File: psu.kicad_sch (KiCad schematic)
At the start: 8 parts, among them J2 USB_C_Receptacle_PowerOnly_6P, Q3 TIP125, Q4 TIP122

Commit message: Progress.
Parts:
- removed C7: 100n, Capacitor_SMD:C_0603_1608Metric_Pad1.08x0.95mm_HandSolder, symbol Device:C
- removed Q3: TIP125, Package_TO_SOT_THT:TO-220-3_Vertical, symbol Transistor_BJT:TIP125
- removed Q4: TIP122, Package_TO_SOT_THT:TO-220-3_Vertical, symbol Transistor_BJT:TIP122
- removed R23, R24: 2k, Resistor_SMD:R_0603_1608Metric_Pad0.98x0.95mm_HandSolder, symbol Device:R_US
- added C10, C11, C12, C13, C16, C20, C21, C24, C7: 47u, Capacitor_THT:CP_Radial_D5.0mm_P2.00mm, symbol Device:C_Polarized_US
- added C14, C15, C17, C18, C19, C22, C23, C8, C9: 1u, Resistor_SMD:R_0603_1608Metric_Pad0.98x0.95mm_HandSolder, symbol Device:C
- added D1: SK16, Diode_SMD:D_SMA_Handsoldering, symbol solar_push_pull_sym_lib:SK16
- added L1, L2: 4.7u, Inductor_THT:L_Radial_D7.5mm_P3.50mm_Fastron_07P, symbol Device:L
- added Q5: BD679, Package_TO_SOT_THT:TO-126-3_Horizontal_TabUp, symbol DS100M06V_linear:BD679
- added Q6: BD680, Package_TO_SOT_THT:TO-126-3_Horizontal_TabUp, symbol DS100M06V_linear:BD680
- added R29, R30: 1k, Resistor_SMD:R_0603_1608Metric_Pad0.98x0.95mm_HandSolder, symbol Device:R
- added R31, R32: 10k, Resistor_SMD:R_0603_1608Metric_Pad0.98x0.95mm_HandSolder, symbol Device:R
- added R33, R34: 33k, Resistor_SMD:R_0603_1608Metric_Pad0.98x0.95mm_HandSolder, symbol Device:R_US
- added R35: 249.9k, Resistor_SMD:R_0603_1608Metric_Pad0.98x0.95mm_HandSolder, symbol Device:R_US
- added U12: L7805, symbol Regulator_Linear:L7805
- added U13: LMR62421XMF, Package_TO_SOT_SMD:SOT-23-5, symbol Regulator_Switching:LMR62421XMF
- added U15: L7905, symbol Regulator_Linear:L7905
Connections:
- net +16.5V: now also C12.1, C14.1, C19.1, C20.1, Q5.3 (E), U12.1 (IN)
- net +20V: now also C16.1, C17.1, C8.1, C9.1, D1.1 (K), Q5.2 (C), Q6.2 (C), R29.2, R30.2, R35.1
- net +VBUS: now also L1.1, U13.4 (EN), U13.5 (VIN)
- net GND: now also R33.1, R34.1, U13.2 (GND)
- new net: C10.1, Q5.1 (B), R29.1, R31.2
- new net: C11.2, Q6.1 (B), R30.1, R32.2
- new net: R33.2, R34.2, R35.2, U13.3 (FB)
- new net: D1.2 (A), L2.2, U13.1 (SW)
- new net: L1.2, L2.1
- new net +5V: C13.1, C18.1, U12.3 (OUT)
- new net -16.5V: C15.1, C21.2, C22.1, C7.2, Q6.3 (E), U15.2 (VI)
- new net -5V: C23.1, C24.2, U15.3 (VO)
- new net 0: C10.2, C11.1, C12.2, C13.2, C14.2, C15.2, C16.2, C17.2, C18.2, C19.2, C20.2, C21.1, C22.2, C23.2, C24.1, C7.1, C8.2, C9.2, R31.1, R32.1, U12.2 (GND), U15.1 (GND)
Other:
- note added: "20V boost converter"
- note added: "Linear to -16.5V"
- note added: "Linear to -5V"
- note added: "Linear to 16.5V"
- note added: "Linear to 5V"
- note added: "Power input"
- moved on the sheet: J2, R21, R22

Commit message: Savegame.
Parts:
- added C36, C37: 1u, Resistor_SMD:R_0603_1608Metric_Pad0.98x0.95mm_HandSolder, symbol Device:C
- added U14: AP2204K-3.3, Package_TO_SOT_SMD:SOT-23-5, symbol Regulator_Linear:AP2204K-3.3
- J2: footprint (none) -> Connector_USB:USB_C_Receptacle_GCT_USB4125-xx-x_6P_TopMnt_Horizontal
- Q5, Q6: footprint Package_TO_SOT_THT:TO-126-3_Horizontal_TabUp -> Package_TO_SOT_THT:TO-126-3_Vertical
- U12, U15: footprint (none) -> Package_TO_SOT_THT:TO-220-3_Vertical
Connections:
- net 0 is gone; now on net GND: C10.2, C11.1, C12.2, C13.2, C14.2, C15.2, C16.2, C17.2, C18.2, C19.2, C20.2, C21.1, C22.2, C23.2, C24.1, C7.1, C8.2, C9.2, R31.1, R32.1, U12.2 (GND), U15.1 (GND)
- net +5V: now also C36.1, U14.1 (VIN), U14.3 (EN)
- net GND: now also C36.2, C37.2, U14.2 (GND)
- new net +3.3V: C37.1, U14.5 (VOUT)
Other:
- note added: "Linear to 3.3V"
- moved on the sheet: C18, C23

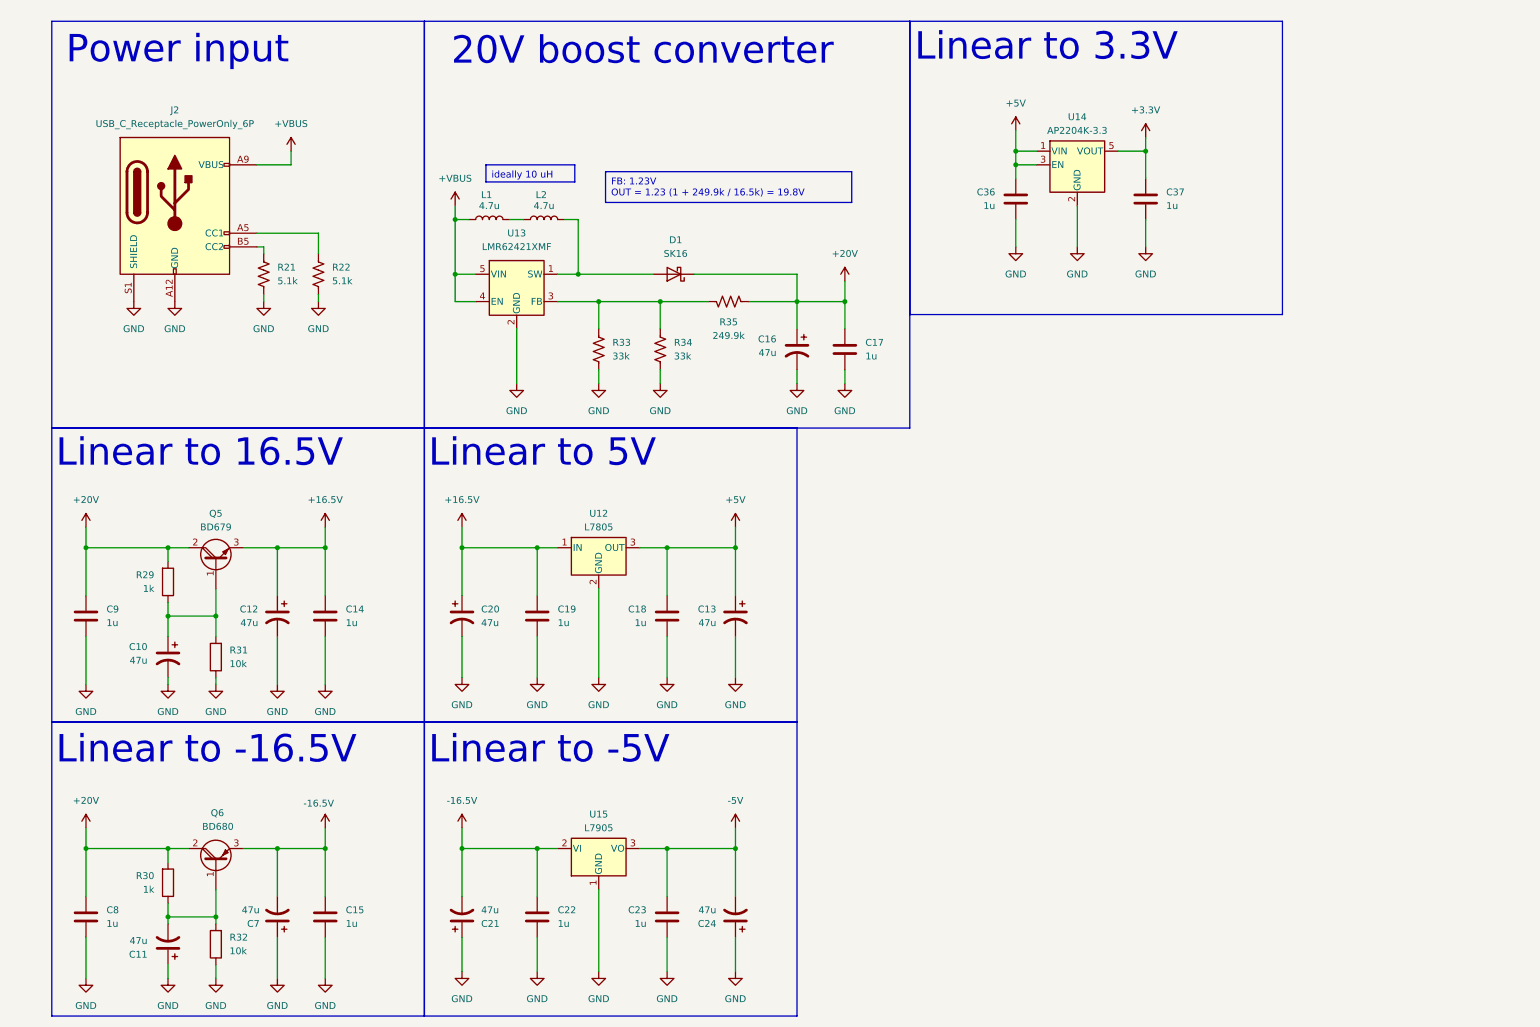
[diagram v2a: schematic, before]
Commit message: SEPIC and CUK
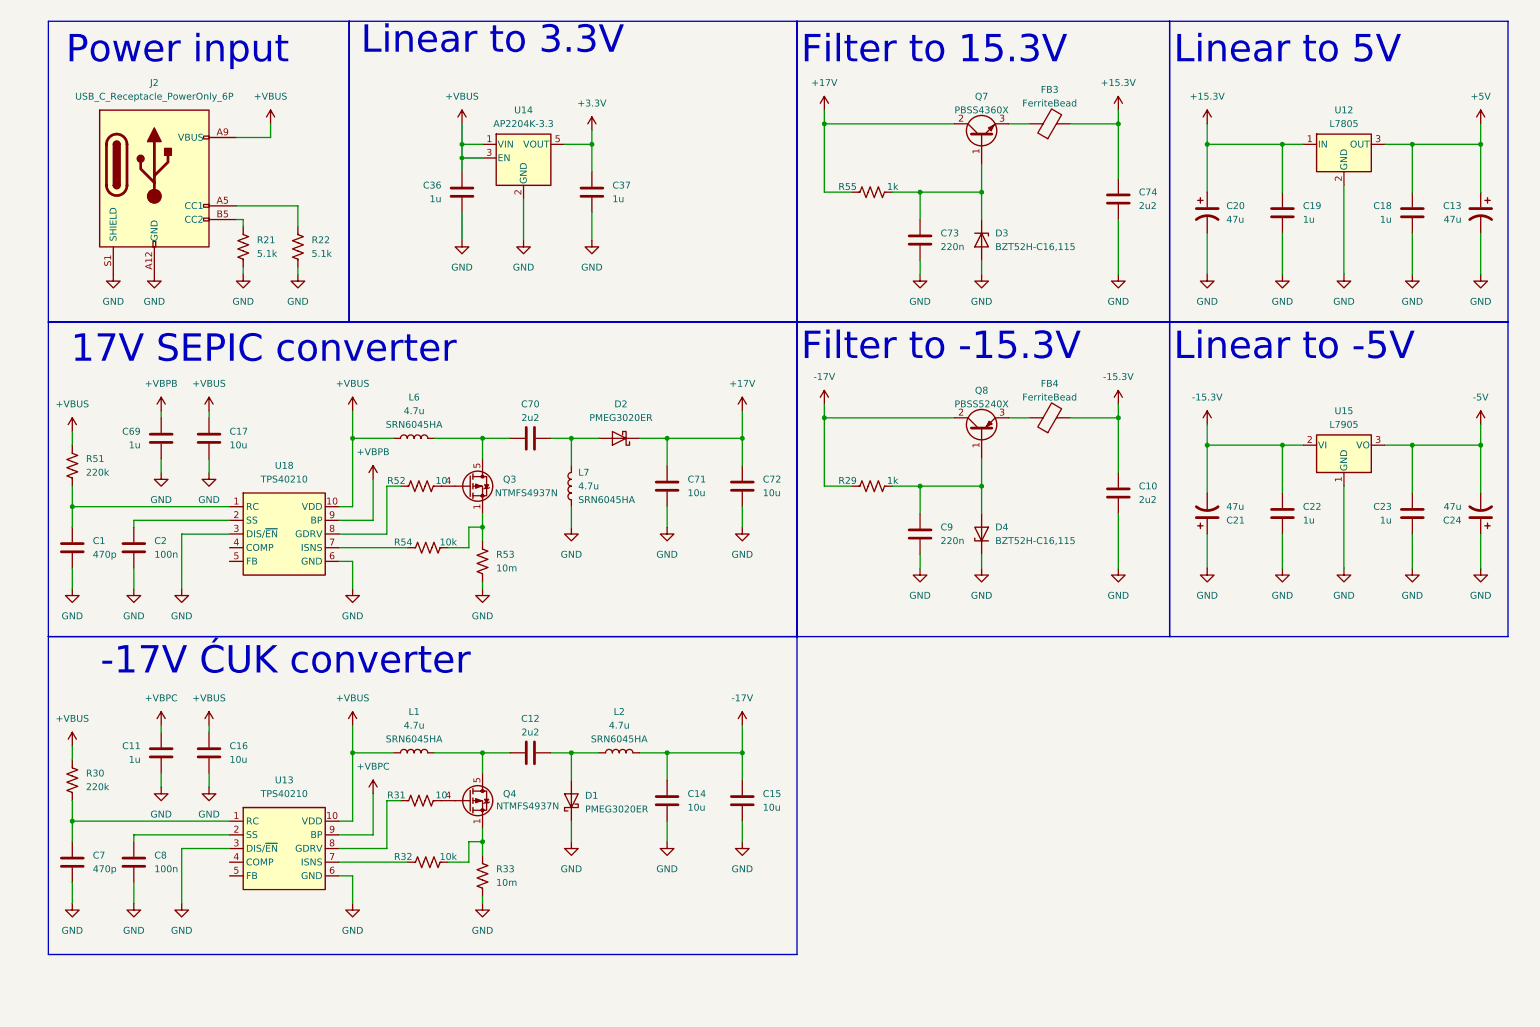
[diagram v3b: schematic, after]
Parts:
- removed C10, C11, C12, C16, C7: 47u, Capacitor_THT:CP_Radial_D5.0mm_P2.00mm, symbol Device:C_Polarized_US
- removed D1: SK16, Diode_SMD:D_SMA_Handsoldering, symbol solar_push_pull_sym_lib:SK16
- removed L1, L2: 4.7u, Inductor_THT:L_Radial_D7.5mm_P3.50mm_Fastron_07P, symbol Device:L
- removed Q5: BD679, Package_TO_SOT_THT:TO-126-3_Vertical, symbol DS100M06V_linear:BD679
- removed Q6: BD680, Package_TO_SOT_THT:TO-126-3_Vertical, symbol DS100M06V_linear:BD680
- removed R29, R30: 1k, Resistor_SMD:R_0603_1608Metric_Pad0.98x0.95mm_HandSolder, symbol Device:R
- removed R31, R32: 10k, Resistor_SMD:R_0603_1608Metric_Pad0.98x0.95mm_HandSolder, symbol Device:R
- removed R34: 33k, Resistor_SMD:R_0603_1608Metric_Pad0.98x0.95mm_HandSolder, symbol Device:R_US
- removed R35: 249.9k, Resistor_SMD:R_0603_1608Metric_Pad0.98x0.95mm_HandSolder, symbol Device:R_US
- removed U13: LMR62421XMF, Package_TO_SOT_SMD:SOT-23-5, symbol Regulator_Switching:LMR62421XMF
- added C1, C7: 470p, Resistor_SMD:R_0603_1608Metric_Pad0.98x0.95mm_HandSolder, symbol Device:C
- added C10, C12, C70, C74: 2u2, Resistor_SMD:R_1206_3216Metric_Pad1.30x1.75mm_HandSolder, symbol Device:C
- added C11, C69: 1u, Resistor_SMD:R_0603_1608Metric_Pad0.98x0.95mm_HandSolder, symbol Device:C
- added C16, C71, C72: 10u, Resistor_SMD:R_1206_3216Metric, symbol Device:C
- added C2: 100n, Resistor_SMD:R_0603_1608Metric_Pad0.98x0.95mm_HandSolder, symbol Device:C
- added C73: 220n, Resistor_SMD:R_0603_1608Metric_Pad0.98x0.95mm_HandSolder, symbol Device:C
- added D1, D2: PMEG3020ER, Diode_SMD:D_SOD-128, symbol Diode:PMEG3020ER
- added D3, D4: BZT52H-C16,115, Diode_SMD:D_SOD-123F, symbol Diode:BZV55C62
- added FB3, FB4: FerriteBead, symbol Device:FerriteBead
- added L1, L2, L6, L7: 4.7u, Inductor_SMD:L_Bourns_SRN6045TA, symbol solar_push_pull_sym_lib:SRN6045HA-4R7Y
- added Q3, Q4: NTMFS4937N, Package_SO:PowerPAK_SO-8_Single, symbol Transistor_FET:DMP3013SFV
- added Q7: PBSS4360X, Package_TO_SOT_SMD:SOT-89-3, symbol Transistor_BJT:KTD1624
- added Q8: PBSS5240X, Package_TO_SOT_SMD:SOT-89-3, symbol Transistor_BJT:BCX52
- added R29, R55: 1k, Resistor_SMD:R_0603_1608Metric_Pad0.98x0.95mm_HandSolder, symbol Device:R_US
- added R30, R51: 220k, Resistor_SMD:R_0603_1608Metric_Pad0.98x0.95mm_HandSolder, symbol Device:R_US
- added R31, R52: 10, Resistor_SMD:R_0603_1608Metric_Pad0.98x0.95mm_HandSolder, symbol Device:R_US
- added R32, R54: 10k, Resistor_SMD:R_0603_1608Metric_Pad0.98x0.95mm_HandSolder, symbol Device:R_US
- added R53: 10m, Resistor_SMD:R_2512_6332Metric_Pad1.40x3.35mm_HandSolder, symbol Device:R_US
- added U13, U18: TPS40210, Package_SO:HVSSOP-10-1EP_3x3mm_P0.5mm_EP1.57x1.88mm, symbol PSG:TPS40210
- C14, C15, C17: value 1u -> 10u; footprint Resistor_SMD:R_0603_1608Metric_Pad0.98x0.95mm_HandSolder -> Resistor_SMD:R_1206_3216Metric
- C8: value 1u -> 100n
- C9: value 1u -> 220n
- R33: value 33k -> 10m; footprint Resistor_SMD:R_0603_1608Metric_Pad0.98x0.95mm_HandSolder -> Resistor_SMD:R_2512_6332Metric_Pad1.40x3.35mm_HandSolder
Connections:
- net +5V: no longer C36.1, U14.1 (VIN), U14.3 (EN)
- net +VBUS: now also C17.1, C36.1, U14.1 (VIN), U14.3 (EN), C16.1, L1.1, L6.1, R30.2, R51.2, U13.10 (VDD), U18.10 (VDD)
- net GND: now also R33.2, C1.2, C10.1, C11.2, C16.2, C2.2, C69.2, C7.2, C71.2, C72.2, C73.2, C74.1, D1.1 (K), D3.2 (A), D4.1 (K), L7.1, R53.2, U13.3 (DIS/~{EN}), U13.6 (GND), U18.3 (DIS/~{EN}), U18.6 (GND); no longer R33.1
- net +16.5V renamed +15.3V
- net +15.3V: now also C74.2, FB3.2; no longer C14.1
- removed net +20V: C17.1, C8.1, C9.1
- net -16.5V renamed -15.3V
- net -15.3V: now also C10.2, FB4.2; no longer C15.1
- new net: C73.1, D3.1 (K), Q7.1 (B), R55.1
- new net: C8.1, U13.2 (SS)
- new net: Q3.4 (G), R52.1
- new net: R52.2, U18.8 (GDRV)
- new net: Q4.1 (S), Q4.2 (S), Q4.3 (S), R32.1, R33.1
- new net: R32.2, U13.7 (ISNS)
- new net: FB3.1, Q7.3 (E)
- new net: C9.1, D4.2 (A), Q8.1 (B), R29.1
- new net: FB4.1, Q8.3 (E)
- new net: C12.2, D1.2 (A), L2.1
- new net: Q3.1 (S), Q3.2 (S), Q3.3 (S), R53.1, R54.1
- new net: C70.1, L6.2, Q3.5 (D)
- new net: C7.1, R30.1, U13.1 (RC)
- new net: R31.2, U13.8 (GDRV)
- new net: C70.2, D2.2 (A), L7.2
- new net: Q4.4 (G), R31.1
- new net: C12.1, L1.2, Q4.5 (D)
- new net: R54.2, U18.7 (ISNS)
- new net: C2.1, U18.2 (SS)
- new net: C1.1, R51.1, U18.1 (RC)
- new net +17V: C71.1, C72.1, D2.1 (K), Q7.2 (C), R55.2
- new net +VBPB: C69.1, U18.9 (BP)
- new net +VBPC: C11.1, U13.9 (BP)
- new net -17V: C14.1, C15.1, L2.2, Q8.2 (C), R29.2
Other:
- note added: "-17V ĆUK converter"
- note added: "17V SEPIC converter"
- note added: "Filter to -15.3V"
- note added: "Filter to 15.3V"
- note removed: "20V boost converter"
- note removed: "Linear to -16.5V"
- note removed: "Linear to 16.5V"
- moved on the sheet: C13, C18, C19, C20, C21, C22, C23, C24, C36, C37, J2, R21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
